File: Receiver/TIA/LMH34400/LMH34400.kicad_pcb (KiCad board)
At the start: 4 copper layers, 34 x 40 mm, 24 parts, among them J1 TEST, J2 Conn_Coaxial, J3 Vout, J4 N_EN, J5 N_ALC, J6 Conn_Coaxial, U1 XLMH34400IDRLR

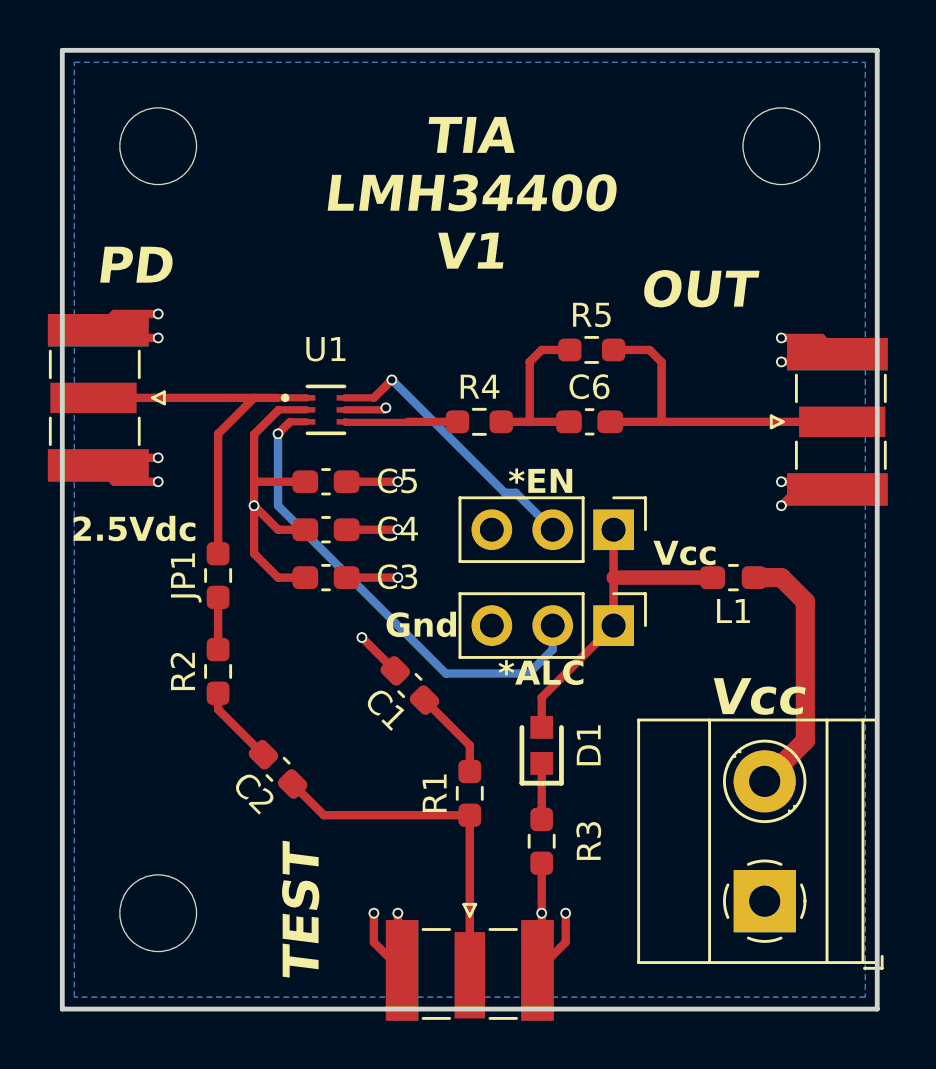
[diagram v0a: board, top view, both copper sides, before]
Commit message: LMH34400 first versio
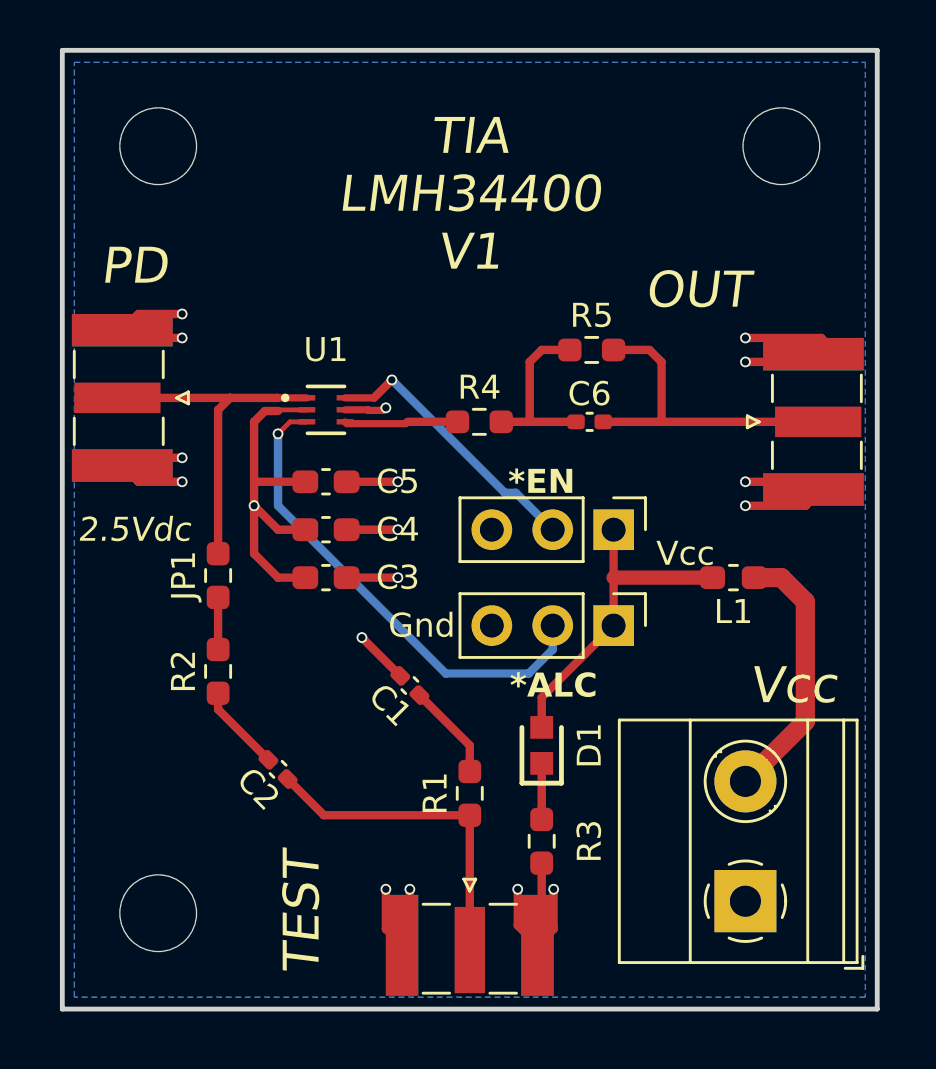
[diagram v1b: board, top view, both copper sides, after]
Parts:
- C1, C2, C6: value 1uF -> .1uF; footprint Capacitor_SMD:C_0603_1608Metric_Pad1.08x0.95mm_HandSolder -> Capacitor_SMD:C_0402_1005Metric_Pad0.74x0.62mm_HandSolder
- D1: value 150060VS75000 -> Green led
- J2: value Conn_Coaxial -> PD IN
- J6: value Conn_Coaxial -> OUT
- L1: value BLM18BA100SN1D -> Ferrite Beads 220 OHM
- R1, R4: value 50 -> 49.9
- U1: value XLMH34400IDRLR -> LMH34400
- moved J1 1.05 mm to (124.0, 90.3)
- moved J2 1.00 mm to (109.5, 67.5)
- moved J6 1.00 mm to (138.3, 68.5)
- moved J3 0.81 mm to (135.5, 88.5)
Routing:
- net GND: track 43.9 -> 50.3 mm
- net Net-(J6-In): track 13.9 -> 12.9 mm

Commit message: LTC6268-10 first version
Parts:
- D1: footprint LumiCom_TIA:LEDC1608X80N -> LED_SMD:LED_0603_1608Metric
- moved JP1 6.41 mm to (113.5, 68.5)
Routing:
- net Net-(J2-In): track 14.1 -> 7.23 mm
- net Net-(JP1-A): track 2.17 -> 8.59 mm

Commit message: LMH3440 fixed
LMH3440 fixed
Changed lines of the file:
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@@
 			(at 0 -1.43 -90)
 			(layer "F.SilkS")
+			(hide yes)
 			(effects
 				(font
@@
 			)
 		)
-		(property "Datasheet" "https://www.vishay.com/doc?28773"
+		(property "Datasheet" "https://www.vishay.com/doc?20035"
 			(at 0 0 -90)
 			(unlocked yes)
@@
 			)
 		)
-		(property "Description" "1/8Watt 1.2Kohms 1% Commercial Use"
+		(property "Description" " Thick Film Resistors - SMD 1/10watt 1.2Kohms 1% 0603"
 			(at 0 0 -90)
 			(unlocked yes)
@@
 			)
 		)
-		(property "Manufacturer Part Number" "CRCW08051K20FKEAC"
+		(property "Manufacturer Part Number" " CRCW06031K20FKEA "
 			(at 0 0 -90)
 			(unlocked yes)
@@
 			)
 		)
-		(property "Mouser Part Number" " 71-CRCW08051K20FKEAC "
+		(property "Mouser Part Number" " 71-CRCW0603-1.2K-E3 "
 			(at 0 0 -90)
 			(unlocked yes)
